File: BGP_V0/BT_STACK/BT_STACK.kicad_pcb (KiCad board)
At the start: 2 copper layers, 30 x 30 mm, 13 parts, among them P1 CONN_01X05, U1 OPA180

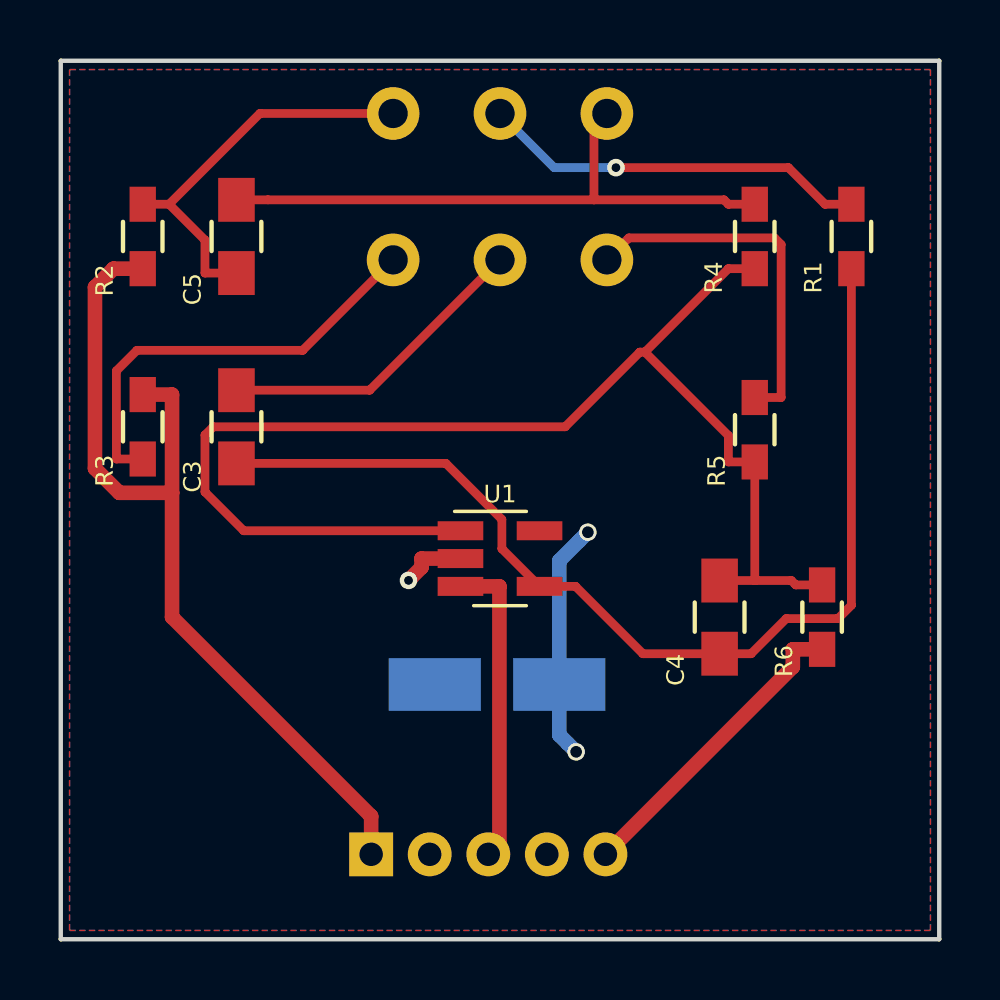
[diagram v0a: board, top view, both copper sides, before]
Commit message: Gerbers
Mainly getting gerbers ready.  Issue with pots overlapping other boards in silk screens - top and bottom.
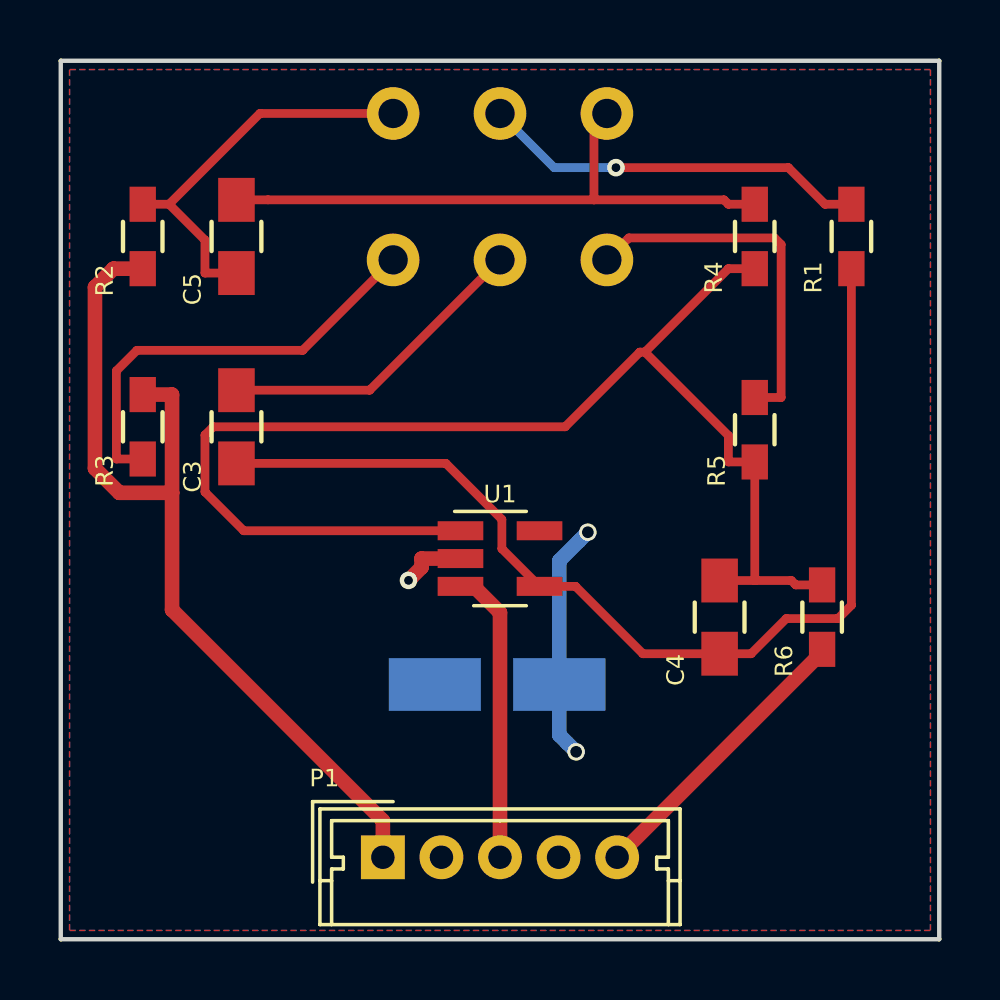
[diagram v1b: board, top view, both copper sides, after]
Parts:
- P1: moved to F.Cu
- moved P1 0.41 mm to (181.0, 95.2)
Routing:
- net /OUT: track 10.7 -> 10.00 mm
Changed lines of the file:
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@@
-(kicad_pcb (version 4) (host pcbnew 4.0.4-1.fc24-product)
+(kicad_pcb (version 4) (host pcbnew 4.0.7)
   (general
     (links 23)
@@
     (pad_to_mask_clearance 0.2)
     (aux_axis_origin 0 0)
-    (visible_elements FFFFFF7F)
+    (visible_elements 7FFFFFFF)
     (pcbplotparams
       (layerselection 0x010f0_80000001)
@@
       (drillshape 0)
       (scaleselection 1)
-      (outputdirectory ../../BGP/GERBER/BT_0/))
+      (outputdirectory ../../GERBER/BT_0/))
   )
   (net 0 "")
@@
     )
     (fp_text user %R (at 0 0 90) (layer F.Fab)
-      (effects (font (size 0.5 0.5) (thickness 0.075)))
+      (effects (font (size 0.6 0.6) (thickness 0.15)))
     )
     (fp_line (start -0.9 1.61) (end 0.9 1.61) (layer F.SilkS) (width 0.12))
@@
     )
     (fp_text user + (at -4.70154 2.4003 180) (layer B.SilkS)
-      (effects (font (size 1 1) (thickness 0.15)) (justify mirror))
+      (effects (font (size 0.6 0.6) (thickness 0.15)) (justify mirror))
     )
     (fp_line (start -4.20116 1.89992) (end -4.20116 -1.89992) (layer B.SilkS) (width 0.15))
@@
     )
   )
-  (module Connectors_Molex:Molex_MicroLatch-53253-0570_05x2.00mm_Straight (layer B.Cu)
-    (at 180.6 95.1)
+  (module Connectors_Molex:Molex_MicroLatch-53253-0570_05x2.00mm_Straight (layer F.Cu)
+    (at 181 95.2)
     (descr "Molex Micro-Latch connector, PN:53253-0570, top entry type, through hole")
     (tags "conn molex micro latch")
-    (fp_text reference P1 (at -1.6 2.175001) (layer B.SilkS)
-      (effects (font (size 0.6 0.6) (thickness 0.15)) (justify mirror))
-    )
-    (fp_text value CONN_01X05 (at 4 3.5) (layer B.Fab) hide
-      (effects (font (size 0.6 0.6) (thickness 0.15)) (justify mirror))
-    )
-    (fp_line (start -2.6 2.1) (end -2.6 -2.75) (layer B.CrtYd) (width 0.05))
-    (fp_line (start -2.6 -2.75) (end 10.55 -2.75) (layer B.CrtYd) (width 0.05))
-    (fp_line (start 10.55 -2.75) (end 10.55 2.1) (layer B.CrtYd) (width 0.05))
-    (fp_line (start 10.55 2.1) (end -2.6 2.1) (layer B.CrtYd) (width 0.05))
-    (fp_line (start -2.1 1.6) (end -2.1 -2.25) (layer B.SilkS) (width 0.15))
-    (fp_line (start -2.1 -2.25) (end 10.1 -2.25) (layer B.SilkS) (width 0.15))
-    (fp_line (start 10.1 -2.25) (end 10.1 1.6) (layer B.SilkS) (width 0.15))
-    (fp_line (start 10.1 1.6) (end -2.1 1.6) (layer B.SilkS) (width 0.15))
-    (fp_line (start 0 2) (end -0.3 2.6) (layer B.SilkS) (width 0.15))
-    (fp_line (start -0.3 2.6) (end 0.3 2.6) (layer B.SilkS) (width 0.15))
-    (fp_line (start 0.3 2.6) (end 0 2) (layer B.SilkS) (width 0.15))
-    (fp_line (start -2.1 -0.8) (end -1.7 -0.8) (layer B.SilkS) (width 0.15))
-    (fp_line (start 10.1 -0.8) (end 9.7 -0.8) (layer B.SilkS) (width 0.15))
-    (fp_line (start 4 1.2) (end -1.7 1.2) (layer B.SilkS) (width 0.15))
-    (fp_line (start -1.7 1.2) (end -1.7 0) (layer B.SilkS) (width 0.15))
-    (fp_line (start -1.7 0) (end -1.3 0) (layer B.SilkS) (width 0.15))
-    (fp_line (start -1.3 0) (end -1.3 -0.4) (layer B.SilkS) (width 0.15))
-    (fp_line (start -1.3 -0.4) (end -1.7 -0.4) (layer B.SilkS) (width 0.15))
-    (fp_line (start -1.7 -0.4) (end -1.7 -2.25) (layer B.SilkS) (width 0.15))
-    (fp_line (start 4 1.2) (end 9.7 1.2) (layer B.SilkS) (width 0.15))
-    (fp_line (start 9.7 1.2) (end 9.7 0) (layer B.SilkS) (width 0.15))
-    (fp_line (start 9.7 0) (end 9.3 0) (layer B.SilkS) (width 0.15))
-    (fp_line (start 9.3 0) (end 9.3 -0.4) (layer B.SilkS) (width 0.15))
-    (fp_line (start 9.3 -0.4) (end 9.7 -0.4) (layer B.SilkS) (width 0.15))
-    (fp_line (start 9.7 -0.4) (end 9.7 -2.25) (layer B.SilkS) (width 0.15))
+    (fp_text reference P1 (at -2 -2.7) (layer F.SilkS)
+      (effects (font (size 0.6 0.6) (thickness 0.15)))
+    )
+    (fp_text value CONN_01X05 (at 4 3.4) (layer F.Fab) hide
+      (effects (font (size 0.6 0.6) (thickness 0.15)))
+    )
+    (fp_line (start -2 -1.5) (end -2 2.15) (layer F.Fab) (width 0.1))
+    (fp_line (start -2 2.15) (end 10 2.15) (layer F.Fab) (width 0.1))
+    (fp_line (start 10 2.15) (end 10 -1.5) (layer F.Fab) (width 0.1))
+    (fp_line (start 10 -1.5) (end -2 -1.5) (layer F.Fab) (width 0.1))
+    (fp_line (start -2.6 -2.1) (end -2.6 2.75) (layer F.CrtYd) (width 0.05))
+    (fp_line (start -2.6 2.75) (end 10.65 2.75) (layer F.CrtYd) (width 0.05))
+    (fp_line (start 10.65 2.75) (end 10.65 -2.1) (layer F.CrtYd) (width 0.05))
+    (fp_line (start 10.65 -2.1) (end -2.6 -2.1) (layer F.CrtYd) (width 0.05))
+    (fp_line (start -2.15 -1.65) (end -2.15 2.3) (layer F.SilkS) (width 0.12))
+    (fp_line (start -2.15 2.3) (end 10.15 2.3) (layer F.SilkS) (width 0.12))
+    (fp_line (start 10.15 2.3) (end 10.15 -1.65) (layer F.SilkS) (width 0.12))
+    (fp_line (start 10.15 -1.65) (end -2.15 -1.65) (layer F.SilkS) (width 0.12))
+    (fp_line (start 0.35 -1.9) (end -2.4 -1.9) (layer F.SilkS) (width 0.12))
+    (fp_line (start -2.4 -1.9) (end -2.4 0.85) (layer F.SilkS) (width 0.12))
+    (fp_line (start 0.35 -1.9) (end -2.4 -1.9) (layer F.Fab) (width 0.1))
+    (fp_line (start -2.4 -1.9) (end -2.4 0.85) (layer F.Fab) (width 0.1))
+    (fp_line (start -2.15 0.8) (end -1.75 0.8) (layer F.SilkS) (width 0.12))
+    (fp_line (start 10.15 0.8) (end 9.75 0.8) (layer F.SilkS) (width 0.12))
+    (fp_line (start 4 -1.25) (end -1.75 -1.25) (layer F.SilkS) (width 0.12))
+    (fp_line (start -1.75 -1.25) (end -1.75 0) (layer F.SilkS) (width 0.12))
+    (fp_line (start -1.75 0) (end -1.35 0) (layer F.SilkS) (width 0.12))
+    (fp_line (start -1.35 0) (end -1.35 0.4) (layer F.SilkS) (width 0.12))
+    (fp_line (start -1.35 0.4) (end -1.75 0.4) (layer F.SilkS) (width 0.12))
+    (fp_line (start -1.75 0.4) (end -1.75 2.3) (layer F.SilkS) (width 0.12))
+    (fp_line (start 4 -1.25) (end 9.75 -1.25) (layer F.SilkS) (width 0.12))
+    (fp_line (start 9.75 -1.25) (end 9.75 0) (layer F.SilkS) (width 0.12))
+    (fp_line (start 9.75 0) (end 9.35 0) (layer F.SilkS) (width 0.12))
+    (fp_line (start 9.35 0) (end 9.35 0.4) (layer F.SilkS) (width 0.12))
+    (fp_line (start 9.35 0.4) (end 9.75 0.4) (layer F.SilkS) (width 0.12))
+    (fp_line (start 9.75 0.4) (end 9.75 2.3) (layer F.SilkS) (width 0.12))
+    (fp_text user %R (at 4 1.5) (layer F.Fab) hide
+      (effects (font (size 0.6 0.6) (thickness 0.15)))
+    )
     (pad 1 thru_hole rect (at 0 0) (size 1.5 1.5) (drill 0.8) (layers *.Cu *.Mask)
       (net 3 /IN))
@@
     (pad 5 thru_hole circle (at 8 0) (size 1.5 1.5) (drill 0.8) (layers *.Cu *.Mask)
       (net 10 /OUT))
-    (model Connectors_Molex.3dshapes/Molex_MicroLatch-53253-0570_05x2.00mm_Straight.wrl
+    (model ${KISYS3DMOD}/Connectors_Molex.3dshapes/Molex_MicroLatch-53253-0570_05x2.00mm_Straight.wrl
       (at (xyz 0 0 0))
       (scale (xyz 1 1 1))
@@
   (segment (start 181.876 85.7452) (end 182.3197 85.3015) (width 0.5) (layer F.Cu) (net 2))
   (segment (start 183.65 85) (end 182.3197 85) (width 0.5) (layer F.Cu) (net 2))
-  (segment (start 180.6 95.1) (end 180.6 93.7997) (width 0.5) (layer F.Cu) (net 3))
+  (segment (start 181 95.2) (end 181 93.95) (width 0.5) (layer F.Cu) (net 3))
+  (segment (start 181 93.95) (end 173.8003 86.7503) (width 0.5) (layer F.Cu) (net 3))
+  (segment (start 173.8003 86.7503) (end 173.8003 82.7539) (width 0.5) (layer F.Cu) (net 3))
   (segment (start 172.8 79.4) (end 173.8003 79.4) (width 0.5) (layer F.Cu) (net 3))
   (segment (start 172.8 75.1) (end 171.7997 75.1) (width 0.5) (layer F.Cu) (net 3))
@@
   (segment (start 171.9993 82.7539) (end 171.1679 81.9225) (width 0.5) (layer F.Cu) (net 3))
   (segment (start 173.8003 82.7539) (end 171.9993 82.7539) (width 0.5) (layer F.Cu) (net 3))
-  (segment (start 173.8003 87) (end 173.8003 82.7539) (width 0.5) (layer F.Cu) (net 3))
-  (segment (start 180.6 93.7997) (end 173.8003 87) (width 0.5) (layer F.Cu) (net 3))
   (segment (start 173.8003 82.7539) (end 173.8003 79.4) (width 0.5) (layer F.Cu) (net 3))
   (segment (start 180.55 79.25) (end 185 74.8) (width 0.3) (layer F.Cu) (net 4))
@@
   (segment (start 176.8003 69.8) (end 173.7003 72.9) (width 0.3) (layer F.Cu) (net 8))
   (segment (start 181.35 69.8) (end 176.8003 69.8) (width 0.3) (layer F.Cu) (net 8))
-  (segment (start 184.9803 94.7197) (end 184.9803 85.95) (width 0.5) (layer F.Cu) (net 9))
+  (segment (start 185 95.2) (end 185 86.845) (width 0.5) (layer F.Cu) (net 9))
+  (segment (start 185 86.845) (end 184.105 85.95) (width 0.5) (layer F.Cu) (net 9))
+  (segment (start 184.105 85.95) (end 183.65 85.95) (width 0.5) (layer F.Cu) (net 9))
   (segment (start 184.6 95.1) (end 184.9803 94.7197) (width 0.5) (layer F.Cu) (net 9))
-  (segment (start 183.65 85.95) (end 184.9803 85.95) (width 0.5) (layer F.Cu) (net 9))
-  (segment (start 194.9997 88.7003) (end 194.9997 88.1) (width 0.5) (layer F.Cu) (net 10))
-  (segment (start 188.6 95.1) (end 194.9997 88.7003) (width 0.5) (layer F.Cu) (net 10))
-  (segment (start 196 88.1) (end 194.9997 88.1) (width 0.5) (layer F.Cu) (net 10))
+  (segment (start 189 95.2) (end 196 88.2) (width 0.5) (layer F.Cu) (net 10))
+  (segment (start 196 88.2) (end 196 88.1) (width 0.5) (layer F.Cu) (net 10))
   (via (at 188.9593 71.65) (size 0.6) (layers F.Cu B.Cu) (net 11))
   (segment (start 186.85 71.65) (end 188.9593 71.65) (width 0.3) (layer B.Cu) (net 11))

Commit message: Pot fixups for silkscreen overlap
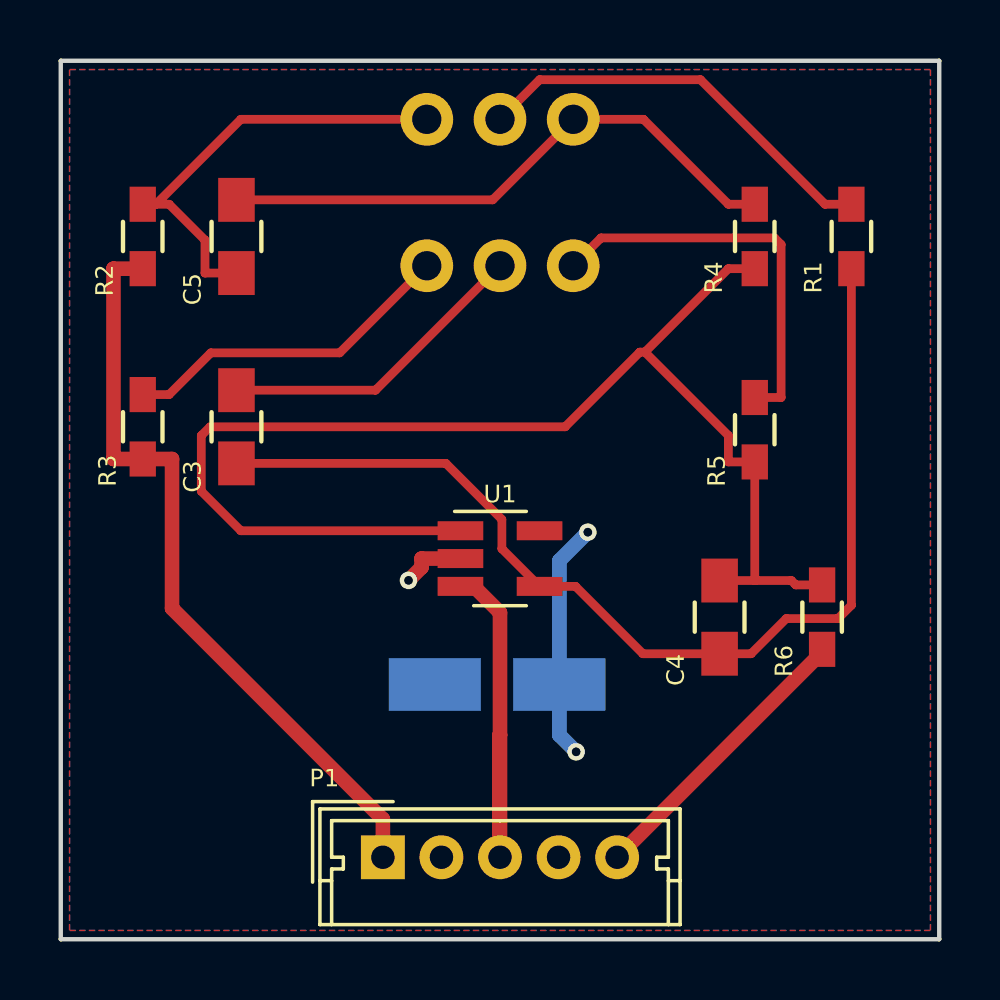
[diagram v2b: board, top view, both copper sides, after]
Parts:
- RV1: footprint LIBS:Potentiometer_Alpha_Double_Vertical_Dual_Shaft -> LIBS:Potentiometer_Alps_RK097_Double_Vertical_Dual_Shaft
- moved RV1 5.66 mm to (182.5, 70.0)
- turned R3 to 270 degrees
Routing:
- net /IN: track 30.8 -> 26.1 mm
- net /REF: track 10.6 -> 14.3 mm
- net /T-: track 14.9 -> 11.5 mm
- net /B-: track 13.8 -> 15.3 mm
- net /T+: track 12.5 -> 13.7 mm
- net /BW: track 13.3 -> 14.3 mm, vias 1 -> 0
- net /B+: track 20.9 -> 20.0 mm

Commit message: Concentric pot fixups for 0_BT Stack and 1_HPF
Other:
- board text added: "BGP V0.0 B/T Stack"
- board text removed: "BGP V1.0 B/T Stack"
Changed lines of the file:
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@@
     (links 23)
     (no_connects 0)
-    (area 169.924999 67.924999 200.075001 98.075001)
+    (area 169.924999 67.424999 200.075001 99.455)
     (thickness 1.6)
     (drawings 9)
@@
     )
   )
-  (gr_text "BGP V1.0\nB/T Stack" (at 196.1 69.8) (layer B.SilkS)
+  (gr_text "BGP V0.0\nB/T Stack" (at 196 70) (layer B.SilkS)
     (effects (font (size 0.6 0.6) (thickness 0.15)) (justify mirror))
   )
